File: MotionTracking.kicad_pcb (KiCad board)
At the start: 2 copper layers, 0 parts

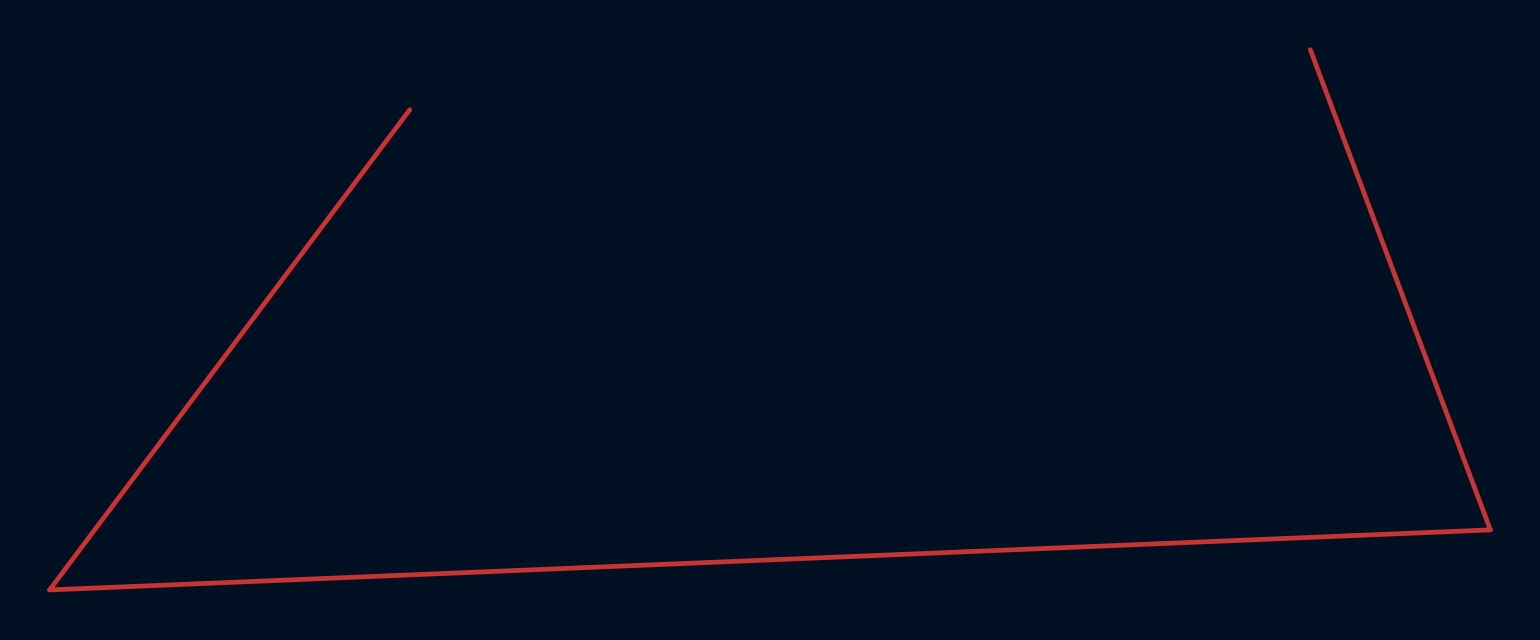
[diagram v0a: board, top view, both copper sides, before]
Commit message: added imu library
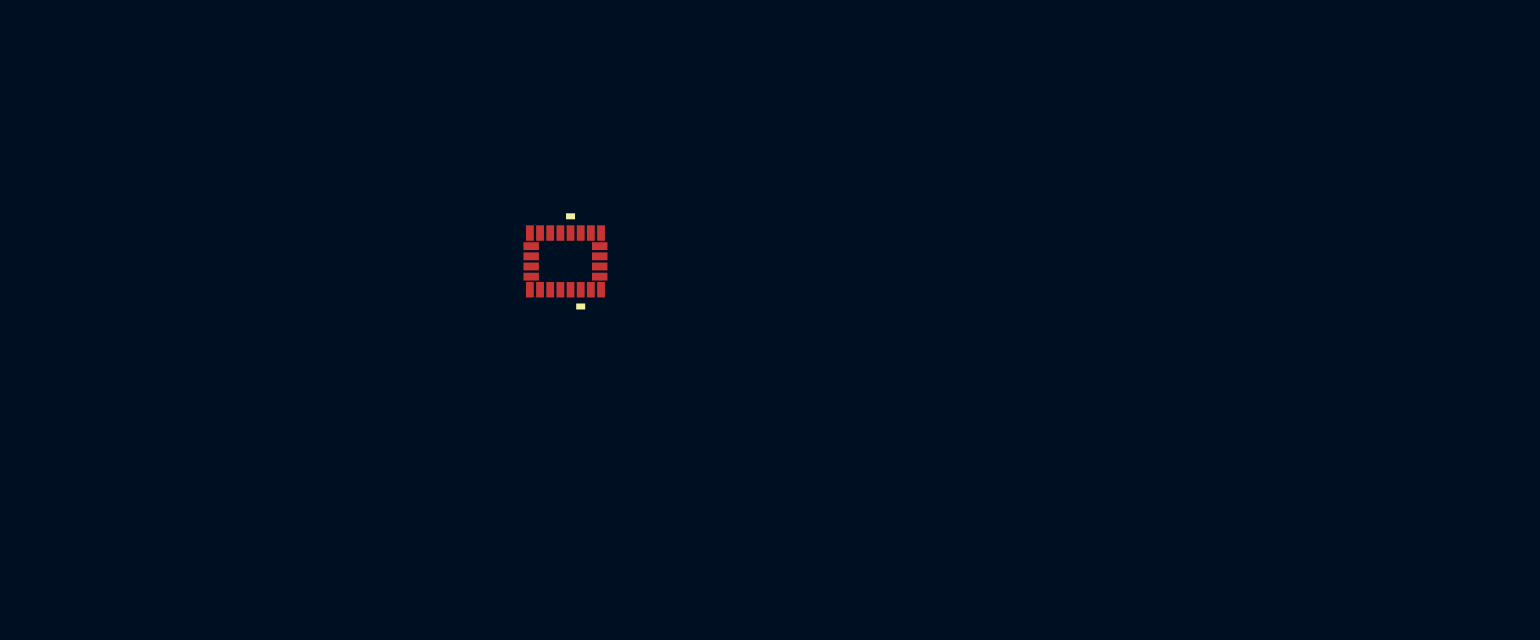
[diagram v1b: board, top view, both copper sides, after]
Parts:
- added poop: LGA-24_3X3P5X1_STM, imu:LGA-24_3X3P5X1_STM, F.Cu at (151.4, 77.5)

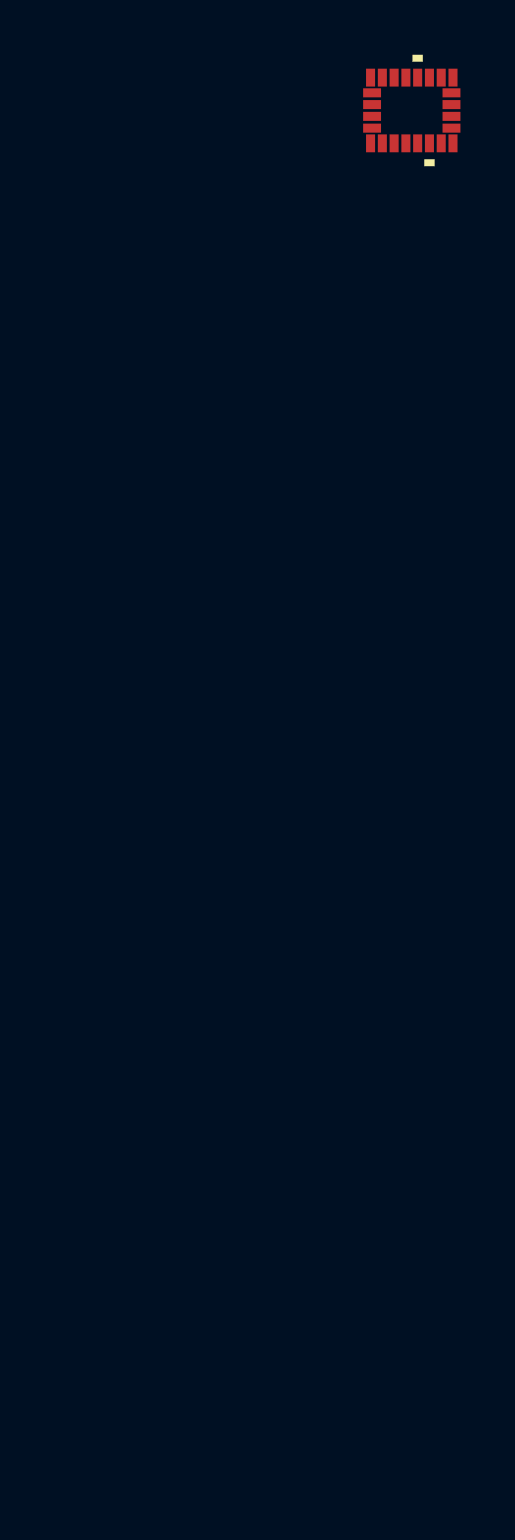
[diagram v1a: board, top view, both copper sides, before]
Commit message: Edited schematic
Added component libraries for stm and imu. Started schematic layout.
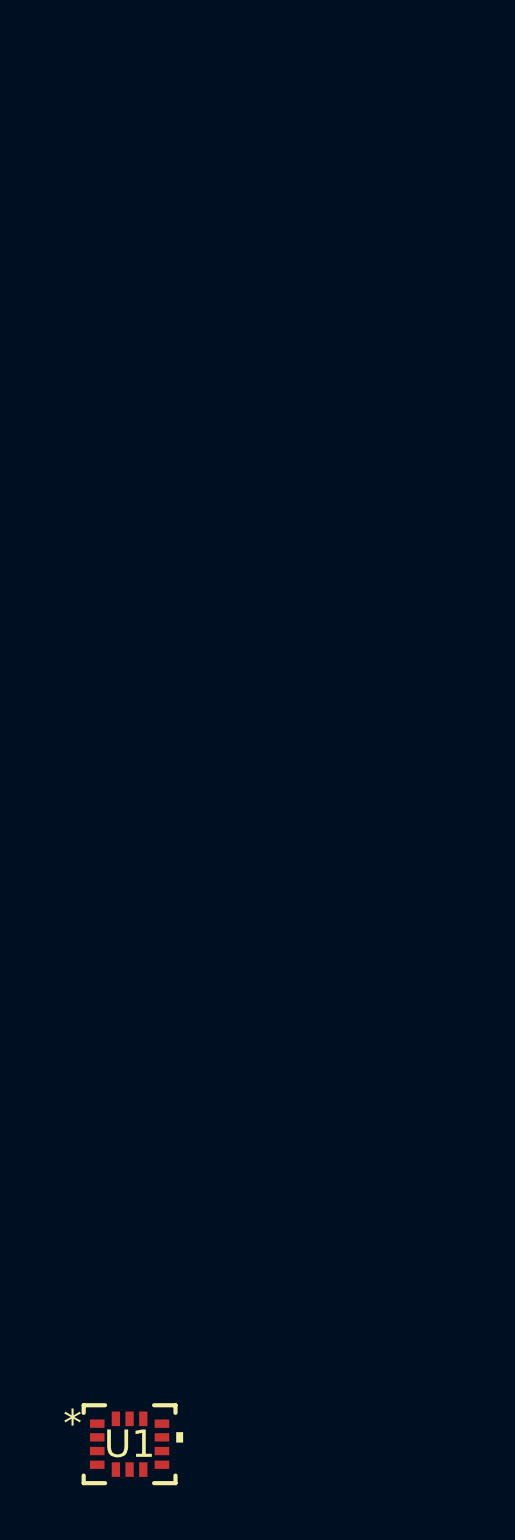
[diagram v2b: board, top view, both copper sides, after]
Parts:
- removed poop: LGA-24_3X3P5X1_STM, imu:LGA-24_3X3P5X1_STM
- added U1: LSM6DSV16XTR, imu:LGA14L_LSM6_STM, F.Cu at (141.1, 126.2)
